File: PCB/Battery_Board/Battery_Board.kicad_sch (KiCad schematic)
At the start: 3 parts

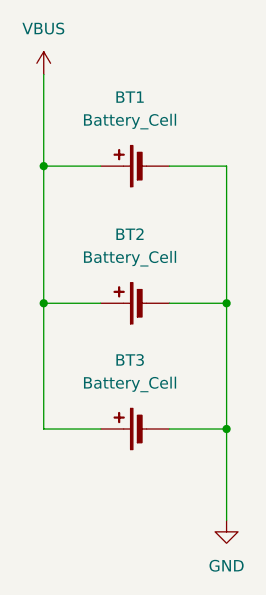
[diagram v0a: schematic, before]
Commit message: changed battery config to series, added graphic
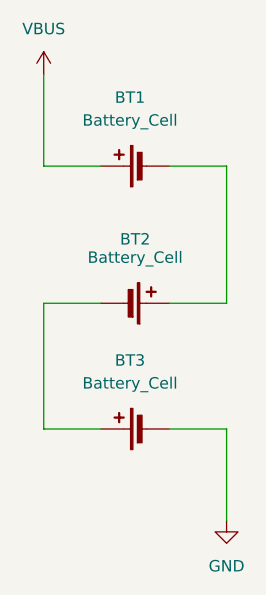
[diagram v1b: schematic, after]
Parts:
- BT1, BT2, BT3: footprint Battery:BatteryHolder_Keystone_1042_1x18650 -> Battery:BatteryHolder_MPD_BK-18650-PC2
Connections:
- net GND: no longer BT1.2 (-), BT2.2 (-)
- net VBUS: no longer BT2.1 (+), BT3.1 (+)
- new net: BT1.2 (-), BT2.1 (+)
- new net: BT2.2 (-), BT3.1 (+)
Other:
- moved on the sheet: BT2
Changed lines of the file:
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@@
 	(generator_version "9.0")
 	(paper "A4")
-	(junction
-		(at 49.53 68.58)
-		(diameter 0)
-		(color 0 0 0 0)
-	)
-	(junction
-		(at 29.21 39.37)
-		(diameter 0)
-		(color 0 0 0 0)
-	)
-	(junction
-		(at 29.21 54.61)
-		(diameter 0)
-		(color 0 0 0 0)
-	)
-	(junction
-		(at 49.53 54.61)
-		(diameter 0)
-		(color 0 0 0 0)
-	)
 	(wire
 		(pts
@@
 		(pts
 			(xy 49.53 68.58) (xy 49.53 78.74)
-		)
-		(stroke
-			(width 0)
-			(type default)
-		)
-	)
-	(wire
-		(pts
-			(xy 49.53 54.61) (xy 49.53 68.58)
-		)
-		(stroke
-			(width 0)
-			(type default)
-		)
-	)
-	(wire
-		(pts
-			(xy 29.21 39.37) (xy 29.21 54.61)
 		)
 		(stroke
@@
 	(symbol
 		(lib_id "Device:Battery_Cell")
-		(at 40.64 54.61 90)
+		(at 38.1 54.61 270)
+		(mirror x)
 		(unit 1)
 		(exclude_from_sim no)
@@
 		(on_board yes)
 		(dnp no)
-		(fields_autoplaced yes)
 		(property "Reference" "BT2"
-			(at 38.7985 46.99 90)
+			(at 39.37 47.498 90)
 			(effects
 				(font
@@
 		)
 		(property "Value" "Battery_Cell"
-			(at 38.7985 49.53 90)
-			(effects
-				(font
-					(size 1.27 1.27)
-				)
-			)
-		)
-		(property "Footprint" "Battery:BatteryHolder_Keystone_1042_1x18650"
-			(at 39.116 54.61 90)
+			(at 39.37 49.53 90)
+			(effects
+				(font
+					(size 1.27 1.27)
+				)
+			)
+		)
+		(property "Footprint" "Battery:BatteryHolder_MPD_BK-18650-PC2"
+			(at 39.624 54.61 90)
 			(effects
 				(font
@@
 		)
 		(property "Datasheet" "~"
-			(at 39.116 54.61 90)
+			(at 39.624 54.61 90)
 			(effects
 				(font
@@
 		)
 		(property "Description" "Single-cell battery"
-			(at 40.64 54.61 0)
+			(at 38.1 54.61 0)
 			(effects
 				(font
@@
 			)
 		)
-		(property "Footprint" "Battery:BatteryHolder_Keystone_1042_1x18650"
+		(property "Footprint" "Battery:BatteryHolder_MPD_BK-18650-PC2"
 			(at 39.116 68.58 90)
 			(effects
@@
 			)
 		)
-		(property "Footprint" "Battery:BatteryHolder_Keystone_1042_1x18650"
+		(property "Footprint" "Battery:BatteryHolder_MPD_BK-18650-PC2"
 			(at 39.116 39.37 90)
 			(effects

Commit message: Added Connector
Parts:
- added J1: SE2-30, SE2-30:SE2-30, symbol SE2-30:SE2-30
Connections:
- net GND: now also J1.29 (GND), J1.30 (GND), J1.59 (GND), J1.60 (GND)
- net VBUS: now also J1.27 (VBus), J1.28 (VBus), J1.57 (VBus), J1.58 (VBus)

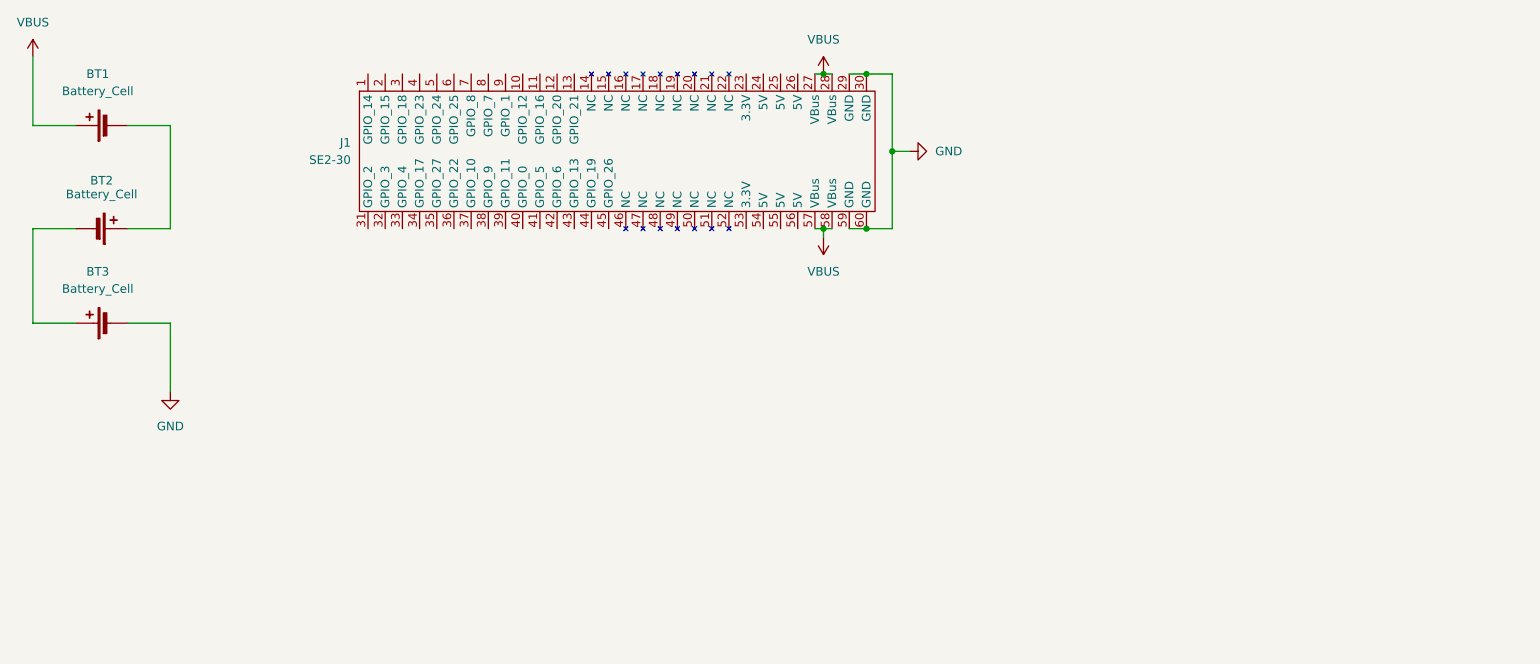
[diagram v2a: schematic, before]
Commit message: Added ideal diode to battery board, cleaned up battery board layout
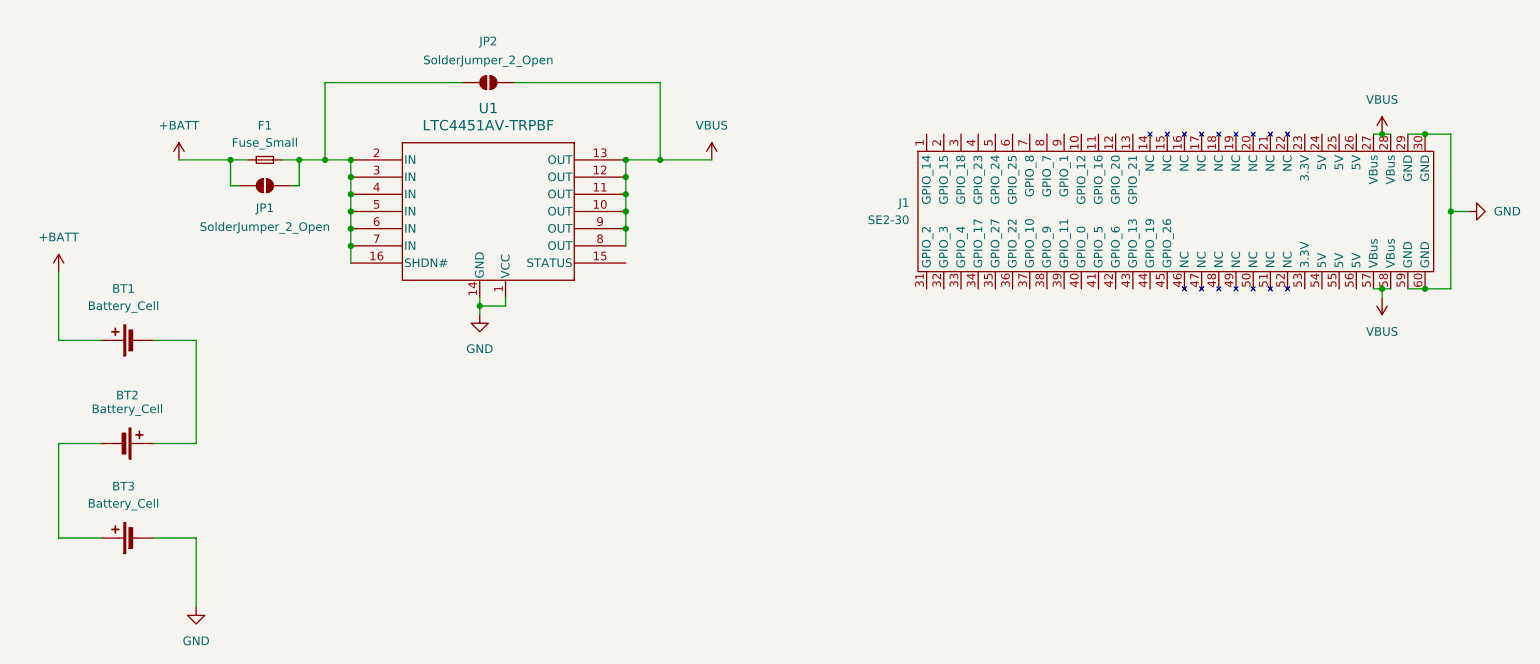
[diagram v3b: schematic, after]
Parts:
- added F1: Fuse_Small, Fuse:Fuse_1206_3216Metric, symbol Device:Fuse_Small
- added JP1, JP2: SolderJumper_2_Open, Jumper:SolderJumper-2_P1.3mm_Open_TrianglePad1.0x1.5mm, symbol Jumper:SolderJumper_2_Open
- added U1: LTC4451AV-TRPBF, SE2-30:05-08-1683_ADI, symbol SE2-30:LTC4451AV-TRPBF
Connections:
- net GND: now also U1.1 (VCC), U1.14 (GND)
- net VBUS: now also JP2.2 (B), U1.10 (OUT), U1.11 (OUT), U1.12 (OUT), U1.13 (OUT), U1.8 (OUT), U1.9 (OUT); no longer BT1.1 (+)
- new net: F1.2, JP1.2 (B), JP2.1 (A), U1.16 (SHDN#), U1.2 (IN), U1.3 (IN), U1.4 (IN), U1.5 (IN), U1.6 (IN), U1.7 (IN)
- new net +BATT: BT1.1 (+), F1.1, JP1.1 (A)
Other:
- moved on the sheet: BT1, BT2, BT3, J1
